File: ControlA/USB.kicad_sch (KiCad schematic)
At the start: 0 parts

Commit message: usb control
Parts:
- added CR?: PUSB3AB6Z, PUSB3AB6Z_NEX, symbol PUSB3AB6Z:PUSB3AB6Z
- added J?: USB_C_Receptacle_USB2.0_16P, symbol Connector:USB_C_Receptacle_USB2.0_16P
- added R? (x5): 0R, symbol Device:R
- added R? (x2): 5K1, symbol Device:R
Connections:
- new net: J?.S1 (SHIELD), R?.1, R?.1
- new net +5V: R?.1
- new net +5V -C: CR?.3 (CH2), CR?.5 (CH4), J?.A4 (VBUS), J?.A9 (VBUS), J?.B4 (VBUS), J?.B9 (VBUS), R?.2
- new net CC1: CR?.4 (CH3), J?.A5 (CC1), R?.1
- new net CC2: CR?.1 (CH1), J?.B5 (CC2), R?.1
- new net GND: CR?.2 (GND), J?.A1 (GND), J?.A12 (GND), J?.B1 (GND), J?.B12 (GND), R?.2, R?.2, R?.2, R?.2
- new net USB-C_N: CR?.6 (CH5), J?.A7 (D-), J?.B7 (D-)
- new net USB-C_P: CR?.7 (CH6), J?.A6 (D+), J?.B6 (D+)
- no-connect marks 0 -> 2
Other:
- note added: "ESD PROTECTION PLACE AS CLOSE AS POSSIBLE TO THE CONNECTOR"
- note added: "MOUNT A OR JUMPER IF USED AS USB HOST"
- note added: "PULL_DOWN TELL THE HOST WE ARE UFP. ONLY ONE USED AT GIVEN TIME. BOTH NECESSARY FOR REVERSIBILITY."
- note added: "ROUTE AS DIFFERENTIAL PAIR"
- note added: "USB"

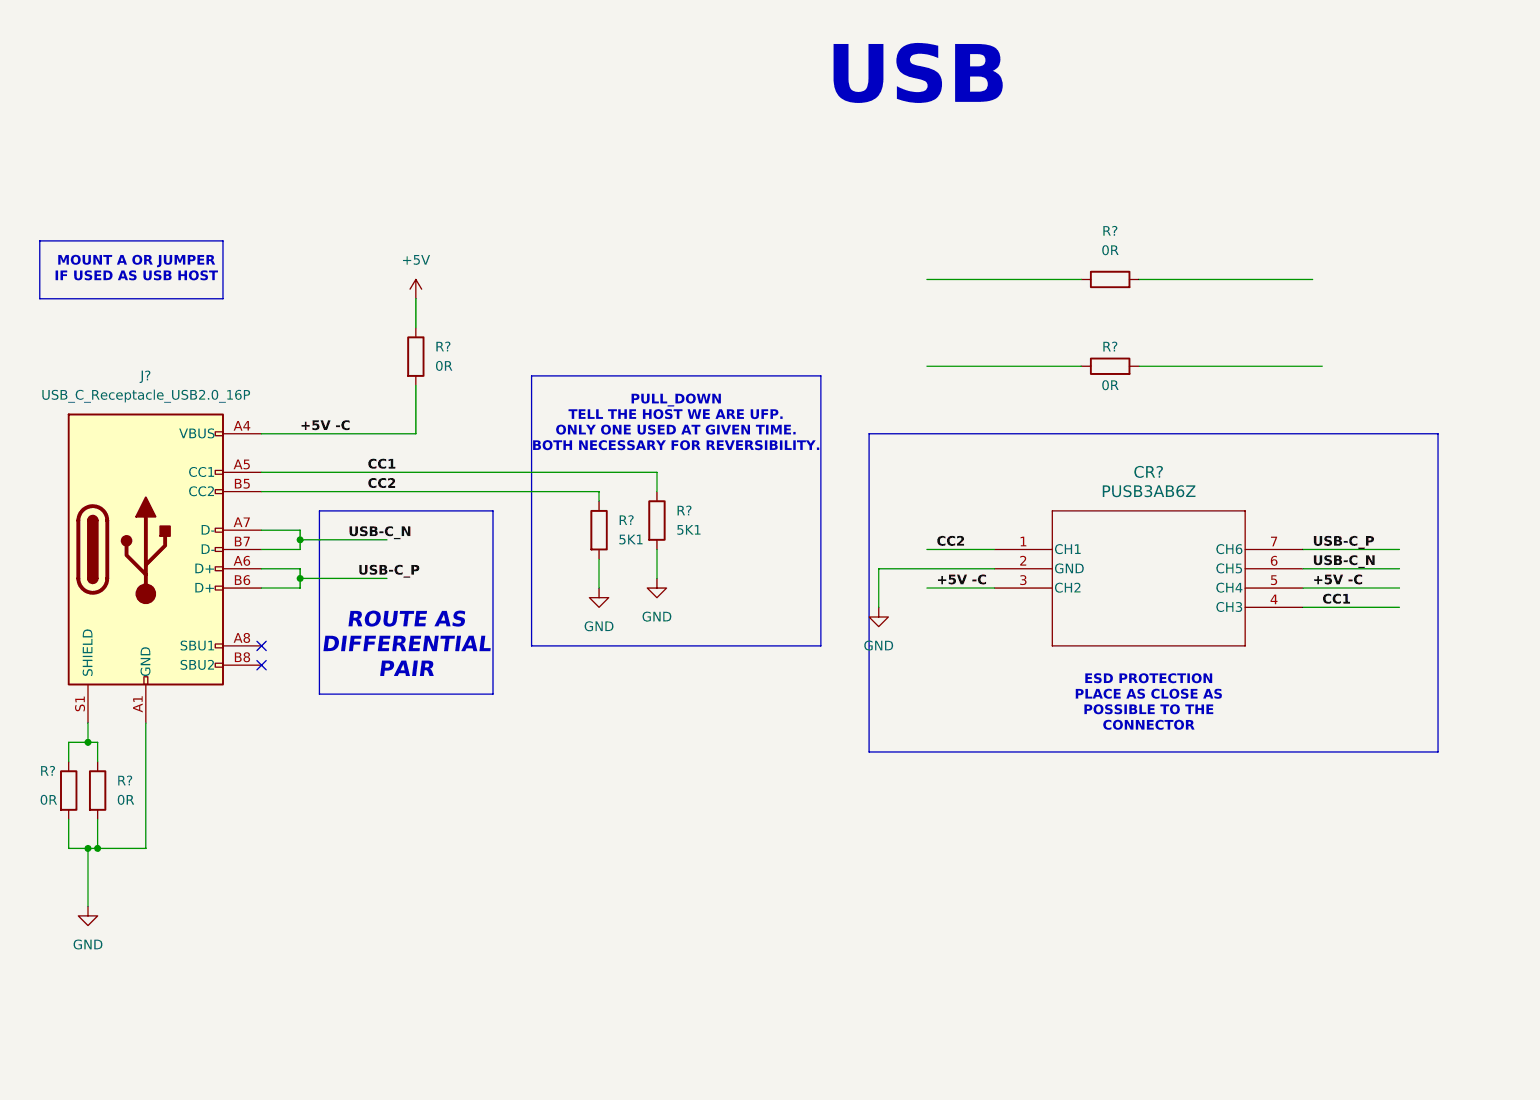
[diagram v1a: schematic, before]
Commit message: final shema symbole
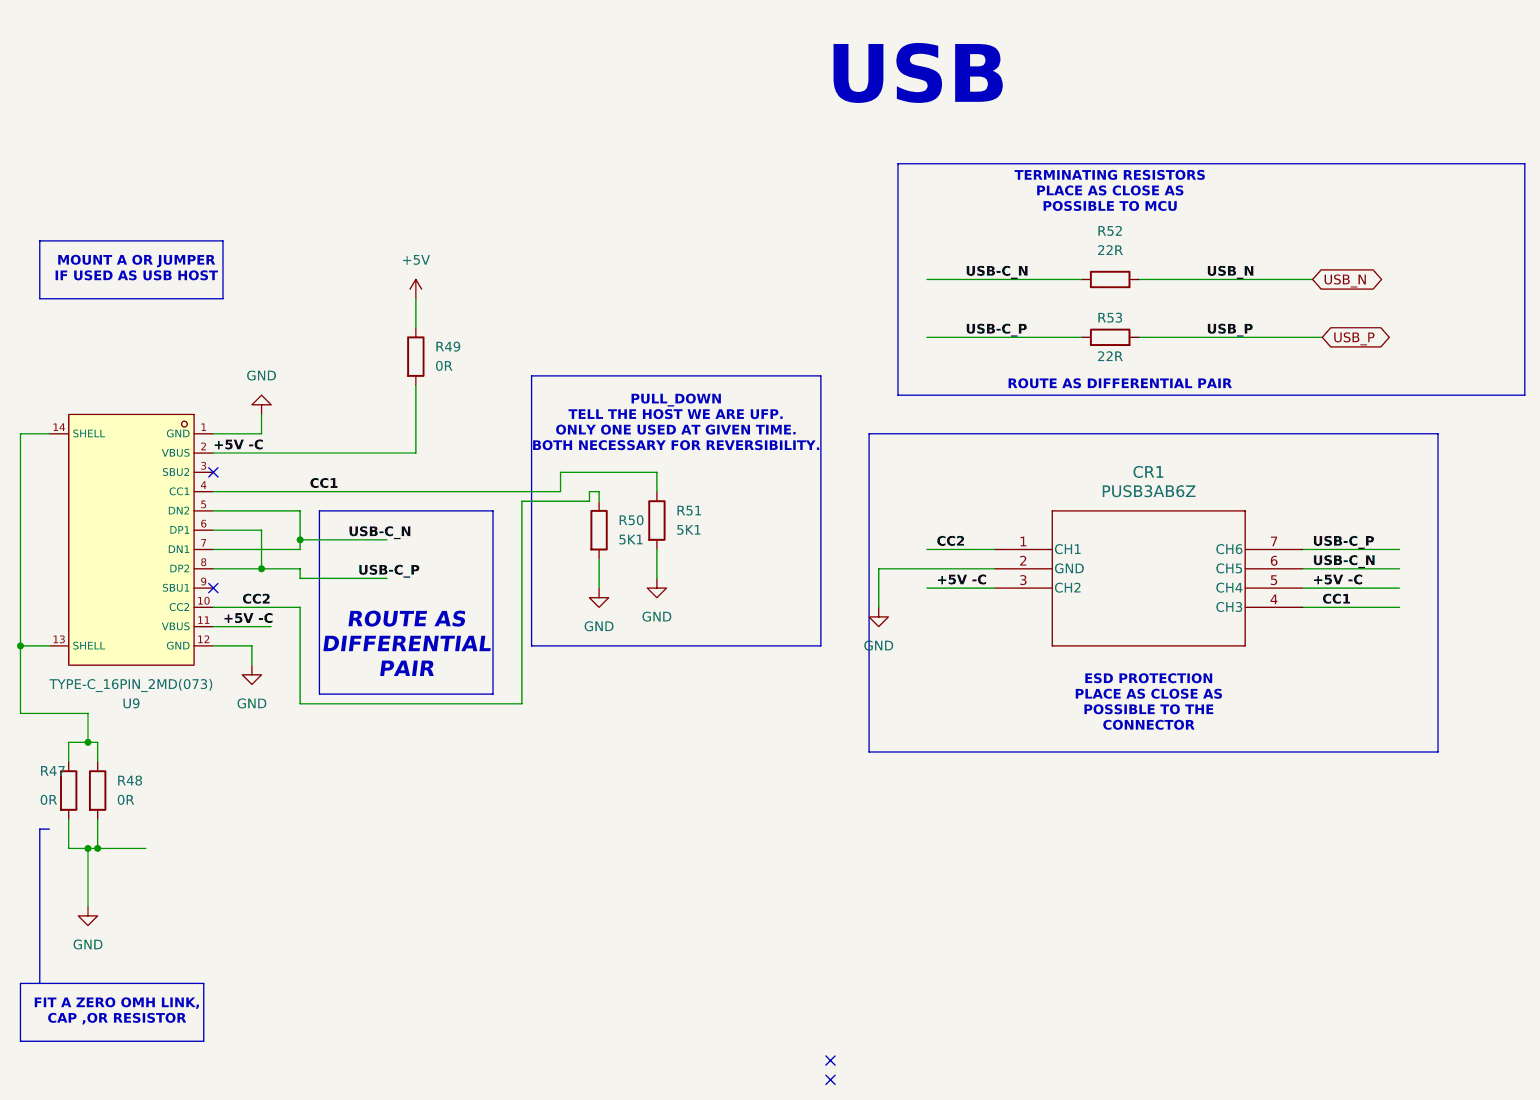
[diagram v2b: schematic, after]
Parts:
- removed J?: USB_C_Receptacle_USB2.0_16P, symbol Connector:USB_C_Receptacle_USB2.0_16P
- added U9: TYPE-C_16PIN_2MD(073), footprint:USB-C-SMD_TYPE-C-6PIN-2MD-073, symbol TYPE-C 16PIN 2MD(073):TYPE-C_16PIN_2MD(073)
- CR1: renamed from CR?; footprint PUSB3AB6Z_NEX -> footprint:PUSB3AB6Z_NEX-M
- R47, R48, R49, R50, R51: renamed from R?; footprint (none) -> Resistor_SMD:R_0805_2012Metric
- R52, R53: renamed from R?; value 0R -> 22R; footprint (none) -> Resistor_SMD:R_0805_2012Metric
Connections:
- net +5V -C: now also U9.11 (VBUS), U9.2 (VBUS)
- net CC1: now also U9.4 (CC1)
- net CC2: now also U9.10 (CC2)
- net GND: now also U9.1 (GND), U9.12 (GND)
- net USB-C_N: now also R52.1, U9.5 (DN2), U9.7 (DN1)
- net USB-C_P: now also R53.1, U9.6 (DP1), U9.8 (DP2)
- net USB_N: now reaches R52.2
- net USB_P: now reaches R53.2
- net at R47.1, R48.1: now also U9.13 (SHELL), U9.14 (SHELL)
- no-connect marks 2 -> 4
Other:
- note added: "FIT A ZERO OMH LINK, CAP ,OR RESISTOR"
- note added: "TERMINATING RESISTORS PLACE AS CLOSE AS POSSIBLE TO MCU"
- moved on the sheet: R53
